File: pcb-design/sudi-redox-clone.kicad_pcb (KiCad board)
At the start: 2 copper layers, 141.8 x 99.4 mm, 143 parts, among them J1 SIDE_CON, J10 ARM_JTAG, J2 0.91 OLED, J4 USBC_PWR_ONLY, J5 SIDE_CON, J6 USB_A, J7 ARMJTAG, J8 BatCon, J9 AVR-ISP-6, K1 KEYSW, K10 KEYSW, K11 KEYSW, K12 KEYSW, K13 KEYSW, K14 KEYSW, K15 KEYSW, K16 KEYSW, K17 KEYSW, K18 KEYSW, K2 KEYSW, K3 KEYSW, K4 KEYSW, K5 KEYSW, K6 KEYSW, K7 KEYSW, K8 KEYSW, K9 KEYSW, SW2 RCV_RST, U1 AMS1117-3.3, U2 ATmega8U2-A, U3 nRF51x22-QFxx, U4 AMS1117-3.3, U5 nRF51x22-QFxx, U6 TP4056, U8 MCP23017_SS, Y2 16MHz, Y3 16MHz, Y4 8MHz

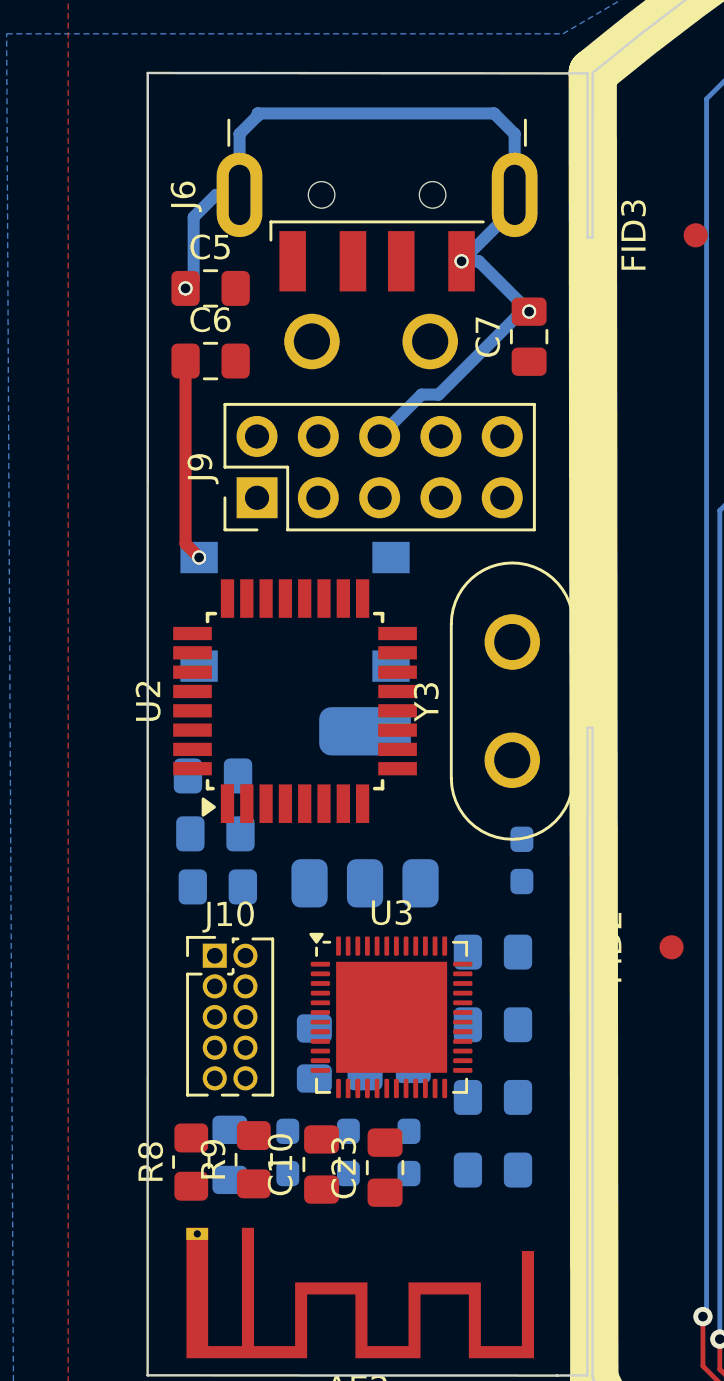
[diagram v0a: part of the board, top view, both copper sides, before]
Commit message: finsihed receiver route
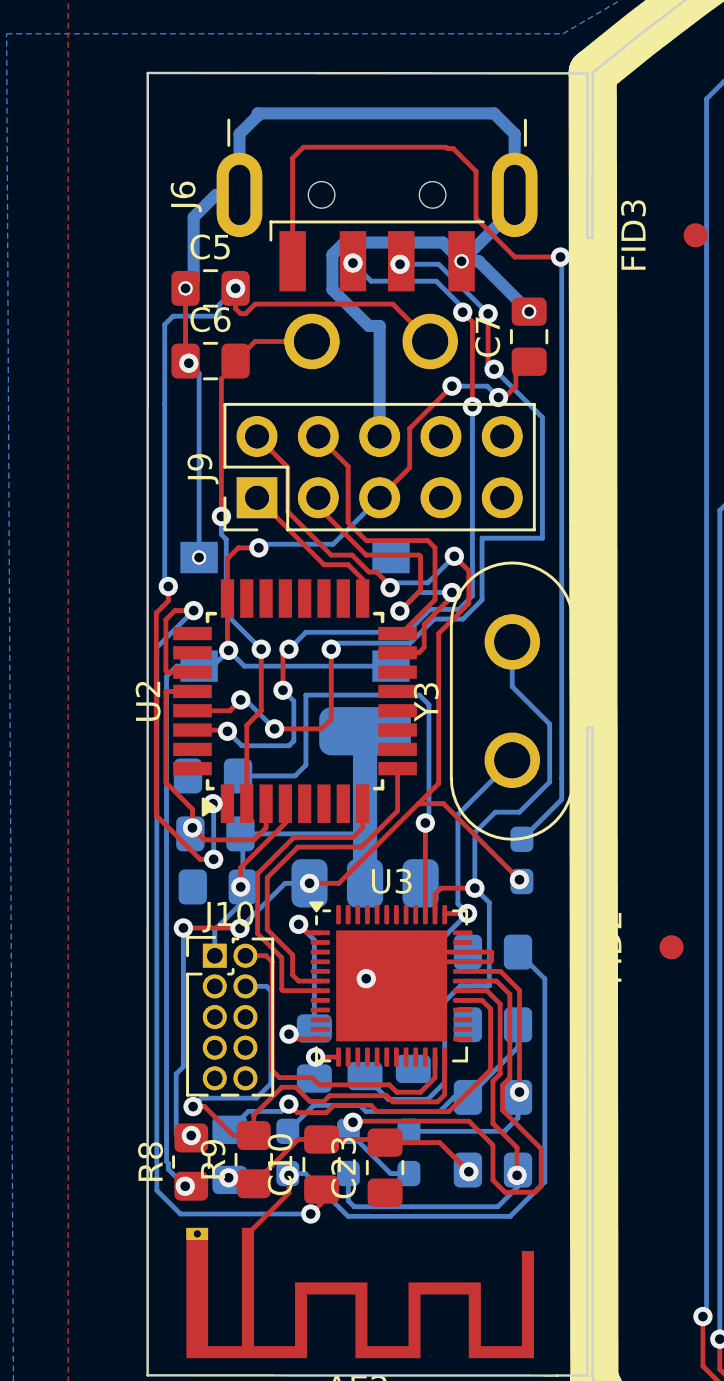
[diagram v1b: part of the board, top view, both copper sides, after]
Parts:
- moved U3 1.30 mm to (61.8, 113.8)
- turned C30 to -90 degrees
- turned L4 to 90 degrees
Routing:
- net /Receiver/RCV_RST: track 0.00 -> 53.0 mm, vias 0 -> 5
- net +5V: track 78.7 -> 129.5 mm, vias 7 -> 14
- net GND: track 738.8 -> 786.5 mm, vias 55 -> 61
- net Net-(J6-VBUS): track 0.00 -> 43.4 mm, vias 0 -> 1
- net Net-(U2-XTAL1): track 0.00 -> 40.4 mm, vias 0 -> 4
- net Net-(U2-UCAP): track 0.00 -> 37.2 mm, vias 0 -> 2
- net Net-(J6-D+): track 0.00 -> 36.5 mm, vias 0 -> 6
- net Net-(J6-D-): track 0.00 -> 34.7 mm, vias 0 -> 6
- net +3.3V: track 194.0 -> 223.6 mm, vias 10 -> 13
- net Net-(U3-XC2): track 0.00 -> 29.1 mm, vias 0 -> 1
- net Net-(AE2-A): track 0.00 -> 25.2 mm, vias 0 -> 1
- net Net-(U3-ANT1): track 0.00 -> 24.4 mm, vias 0 -> 1
- net Net-(U2-PC0/XTAL2): track 0.00 -> 23.0 mm, vias 0 -> 2
- net Net-(J10-SWCLK): track 0.00 -> 23.0 mm, vias 0 -> 1
- net Net-(U3-DEC1): track 0.00 -> 19.9 mm, vias 0 -> 1
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
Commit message: nit
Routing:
- net GND: track 786.5 -> 839.9 mm, vias 61 -> 64
- net Net-(D24-DOUT): track 10.0 -> 40.1 mm, vias 2 -> 5
- net +3.3V: track 223.6 -> 243.8 mm, vias 13 -> 15
- net Net-(D12-DOUT): track 68.2 -> 71.7 mm
- net Net-(U2-PC0/XTAL2): track 23.0 -> 24.0 mm
- net Net-(J10-SWCLK): track 23.0 -> 22.2 mm
- net Net-(U2-XTAL1): track 40.4 -> 41.1 mm
- net /Receiver/RCV_RST: track 53.0 -> 53.7 mm

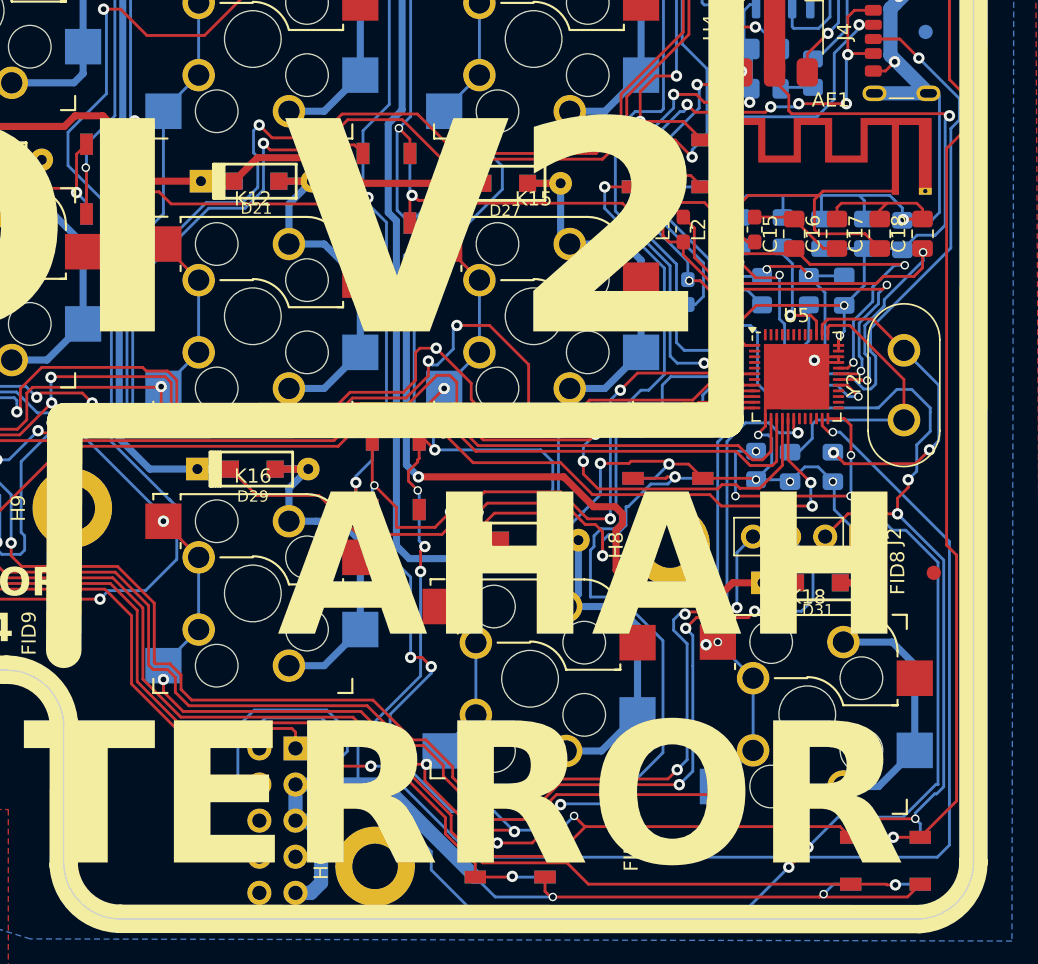
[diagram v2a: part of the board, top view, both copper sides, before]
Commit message: change NRF51822 into NRF52832
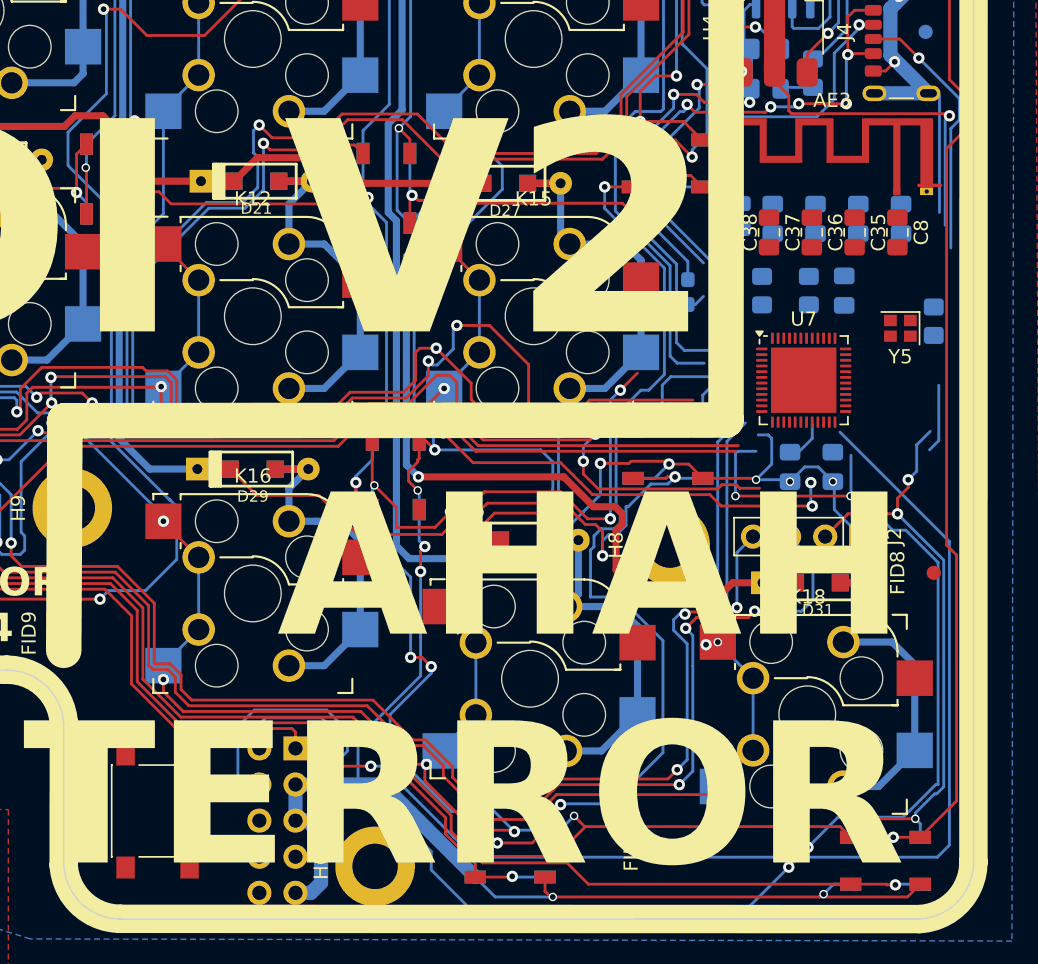
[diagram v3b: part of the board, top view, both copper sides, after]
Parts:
- removed AE1: 2.4GHz, RF_Antenna:Texas_SWRA117D_2.4GHz_Left
- removed C11, C13, C21: 100nF, Capacitor_SMD:C_0805_2012Metric_Pad1.18x1.45mm_HandSolder
- removed C12: 47nF, Capacitor_SMD:C_0805_2012Metric_Pad1.18x1.45mm_HandSolder
- removed C14: 1nF, Capacitor_SMD:C_0805_2012Metric_Pad1.18x1.45mm_HandSolder
- removed C15: 2.2pF, Capacitor_SMD:C_0805_2012Metric_Pad1.18x1.45mm_HandSolder
- removed C16: 1pF, Capacitor_SMD:C_0805_2012Metric_Pad1.18x1.45mm_HandSolder
- removed C17: 1.5p, Capacitor_SMD:C_0805_2012Metric_Pad1.18x1.45mm_HandSolder
- removed C18: 2.2nF, Capacitor_SMD:C_0805_2012Metric_Pad1.18x1.45mm_HandSolder
- removed L1: 10nH, Inductor_SMD:L_0603_1608Metric_Pad1.05x0.95mm_HandSolder
- removed L2: 4.7nH, Inductor_SMD:L_0603_1608Metric_Pad1.05x0.95mm_HandSolder
- removed L3: 3.3nH, Inductor_SMD:L_0603_1608Metric_Pad1.05x0.95mm_HandSolder
- removed R5: 1K, Resistor_SMD:R_0805_2012Metric_Pad1.20x1.40mm_HandSolder
- removed U5: nRF51x22-QFxx, Package_DFN_QFN:QFN-48-1EP_6x6mm_P0.4mm_EP4.6x4.6mm
- removed Y2: 16MHz, Crystal:Crystal_HC50_Vertical
- added AE3: 2.4GHz, RF_Antenna:Texas_SWRA117D_2.4GHz_Left, F.Cu at (188.1, 101.3)
- added C35: 100nF, Capacitor_SMD:C_0805_2012Metric_Pad1.18x1.45mm_HandSolder, F.Cu at (185.1, 104.2)
- added C36: 100nF, Capacitor_SMD:C_0805_2012Metric_Pad1.18x1.45mm_HandSolder, F.Cu at (182.1, 104.2)
- added C37: 1uF, Capacitor_SMD:C_0805_2012Metric_Pad1.18x1.45mm_HandSolder, F.Cu at (179.1, 104.2)
- added C38: 100nF, Capacitor_SMD:C_0805_2012Metric_Pad1.18x1.45mm_HandSolder, F.Cu at (176.1, 104.2)
- added C39: 100nF, Capacitor_SMD:C_0805_2012Metric_Pad1.18x1.45mm_HandSolder, B.Cu at (179.4, 103.2)
- added C40: 100nF/NC, Capacitor_SMD:C_0805_2012Metric_Pad1.18x1.45mm_HandSolder, B.Cu at (182.4, 103.2)
- added C41: 0.8pF, Capacitor_SMD:C_0805_2012Metric_Pad1.18x1.45mm_HandSolder, B.Cu at (185.4, 103.2)
- added C42: 100nF, Capacitor_SMD:C_0805_2012Metric_Pad1.18x1.45mm_HandSolder, B.Cu at (188.4, 103.2)
- added C8: 12pF, Capacitor_SMD:C_0805_2012Metric_Pad1.18x1.45mm_HandSolder, F.Cu at (188.1, 104.2)
- added L7: 3.9nH, Inductor_SMD:L_0603_1608Metric_Pad1.05x0.95mm_HandSolder, B.Cu at (177.3, 103.0)
- added R10: 1K, Resistor_SMD:R_0805_2012Metric_Pad1.20x1.40mm_HandSolder, B.Cu at (190.7, 110.5)
- added SW1: RST, Button_Switch_SMD:SW_Push_1P1T_NO_6x6mm_H9.5mm, F.Cu at (136.1, 144.9)
- added U7: nRF52832-QFxx, Package_DFN_QFN:QFN-48-1EP_6x6mm_P0.4mm_EP4.6x4.6mm, F.Cu at (181.6, 114.6)
- added Y5: 32MHz, Crystal:Crystal_SMD_2016-4Pin_2.0x1.6mm, F.Cu at (188.3, 111.0)
- C20: value 12pF -> 100nF
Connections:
- C20 pad 1: GND -> +3.3V
- C20 pad 2: Net-(U5-XC2) -> GND
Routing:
- net GND: track 839.9 -> 774.9 mm, vias 64 -> 58
- net Net-(U5-VDD_PA): track 35.0 -> 0.00 mm, vias 2 -> 0
- net +3.3V: track 243.8 -> 208.8 mm, vias 15 -> 11
- net Net-(U5-ANT1): track 33.0 -> 0.00 mm, vias 2 -> 0
- net +3V7: track 565.5 -> 540.6 mm
- net Net-(U5-ANT2): track 24.0 -> 0.00 mm, vias 2 -> 0
- net Net-(U5-XC2): track 23.3 -> 0.00 mm, vias 2 -> 0
- net Net-(J4-CC1): track 41.5 -> 18.5 mm
- net Net-(AE1-A): track 22.6 -> 0.00 mm
- net Net-(U5-DEC2): track 19.1 -> 0.00 mm, vias 3 -> 0
- net Net-(U7-XC2): track 19.9 -> 2.96 mm
- net row1: track 316.8 -> 308.2 mm
- net Net-(U5-DEC1): track 8.12 -> 0.00 mm, vias 1 -> 0
- net Net-(C15-Pad2): track 6.72 -> 0.00 mm
- net col3: track 139.3 -> 132.9 mm
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
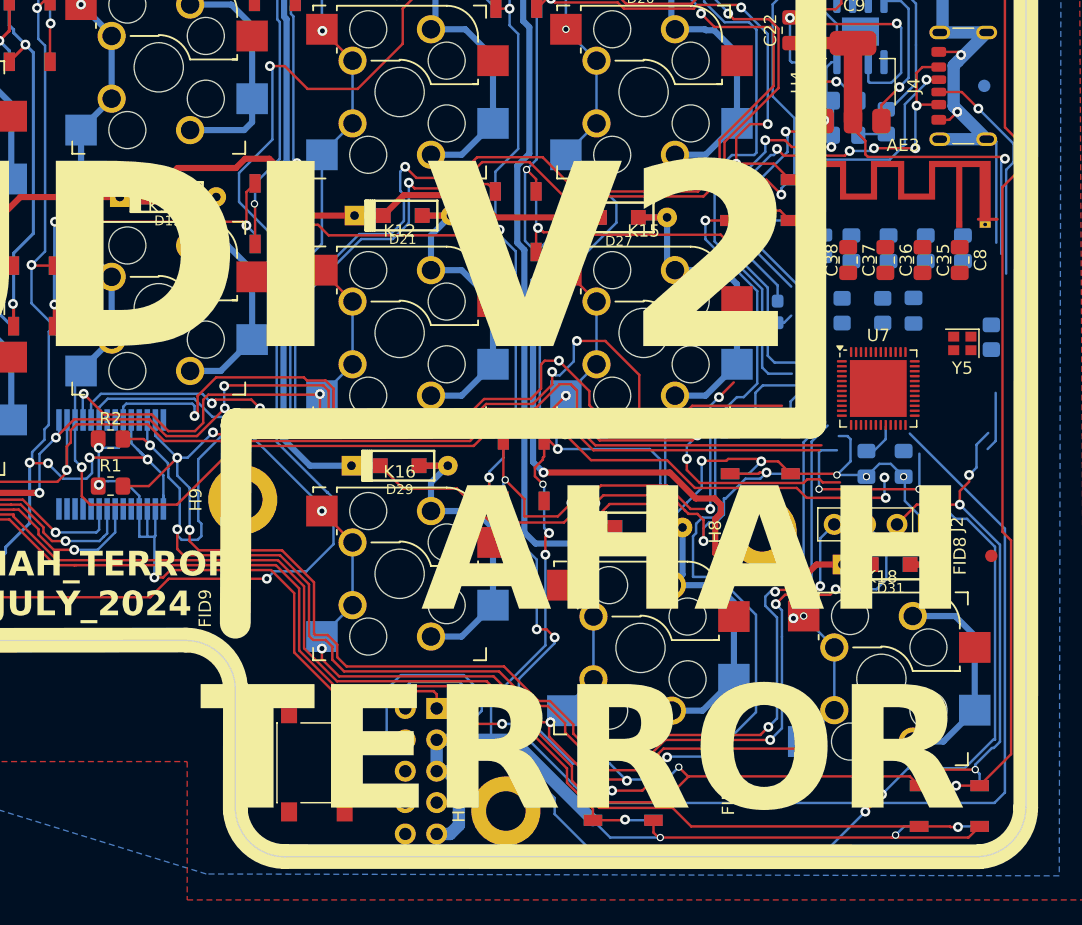
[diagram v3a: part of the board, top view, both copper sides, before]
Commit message: updateRoute to use NRF52832
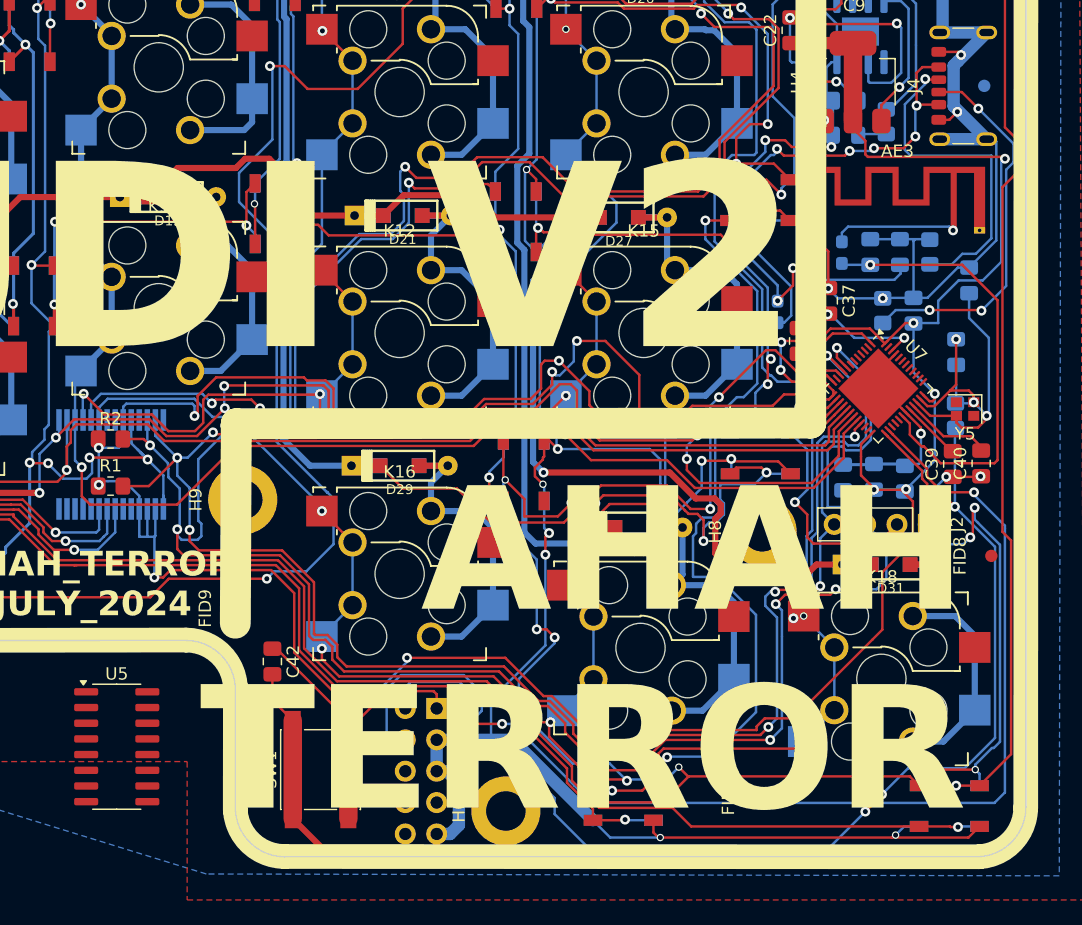
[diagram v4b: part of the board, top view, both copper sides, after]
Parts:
- added U5: CH340G, Package_SO:SOIC-16_3.9x9.9mm_P1.27mm, F.Cu at (119.9, 143.6)
- C35, C36, C8: moved to B.Cu
- C39, C40, C42: moved to F.Cu
- moved C42 65.1 mm to (132.5, 136.7)
- moved C39 19.3 mm to (187.6, 120.7), turned to 90 degrees
- moved C40 19.0 mm to (189.9, 120.7), turned to 90 degrees
- moved C35 18.0 mm to (181.2, 121.8), turned to 90 degrees
- moved C36 17.9 mm to (178.7, 121.8), turned to 90 degrees
- moved C19 11.6 mm to (187.8, 111.7)
- moved C2 8.71 mm to (183.3, 103.5)
- moved R4 8.54 mm to (185.7, 103.5)
- moved R10 6.98 mm to (187.8, 116.8)
- moved C38 6.63 mm to (175.1, 110.8)
- moved Y5 5.32 mm to (188.6, 116.3)
- moved C41 4.50 mm to (180.9, 103.5), turned to 90 degrees
- moved C37 3.67 mm to (177.5, 107.5)
- moved C8 1.82 mm to (188.9, 105.8)
- moved L7 1.37 mm to (178.6, 103.6)
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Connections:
- U7 pad 8: /I2C2_SCL -> SCL
- U7 pad 9: /I2C2_SDA -> SDA
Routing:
- net Net-(U7-P0.21/~{RESET}): track 0.00 -> 89.5 mm, vias 0 -> 2
- net GND: track 774.9 -> 841.6 mm, vias 58 -> 60
- net +3.3V: track 208.8 -> 263.6 mm, vias 11 -> 17
- net Net-(U7-ANT): track 0.00 -> 36.7 mm, vias 0 -> 1
- net SCL: track 222.7 -> 245.7 mm, vias 13 -> 14
- net SDA: track 212.5 -> 233.2 mm, vias 13 -> 14
- net Net-(U7-XC1): track 0.00 -> 18.4 mm, vias 0 -> 1
- net +5V: track 126.4 -> 139.6 mm, vias 12 -> 14
- net Net-(J4-CC1): track 18.5 -> 30.8 mm, vias 1 -> 3
- net row1: track 308.2 -> 318.4 mm
- net Net-(AE3-A): track 0.00 -> 10.1 mm, vias 0 -> 1
- net +3V7: track 540.6 -> 550.6 mm, vias 31 -> 32
- net Net-(U7-DEC4): track 0.00 -> 8.59 mm, vias 0 -> 2
- net Net-(U7-XC2): track 2.96 -> 10.8 mm, vias 0 -> 2
- net Net-(U7-DEC3): track 0.00 -> 7.23 mm
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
